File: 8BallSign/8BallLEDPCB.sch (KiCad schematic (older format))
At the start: 42 parts, among them J101 Solder pads, J102 Solder pads

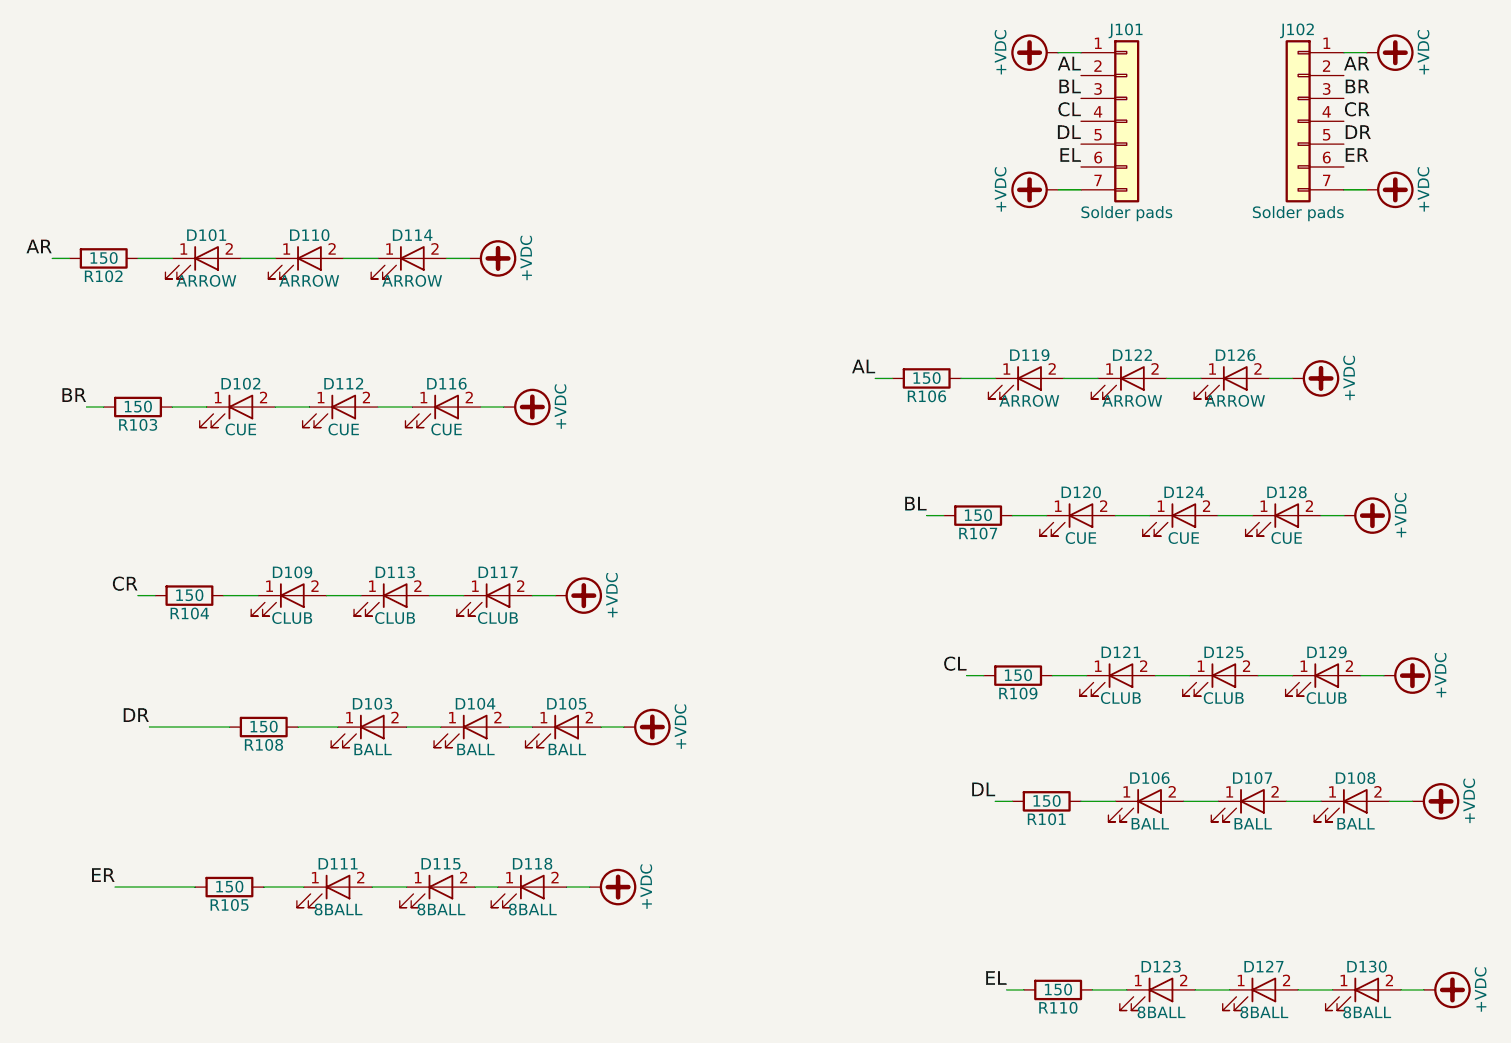
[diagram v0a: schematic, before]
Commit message: Single PCB version (thinner sign).
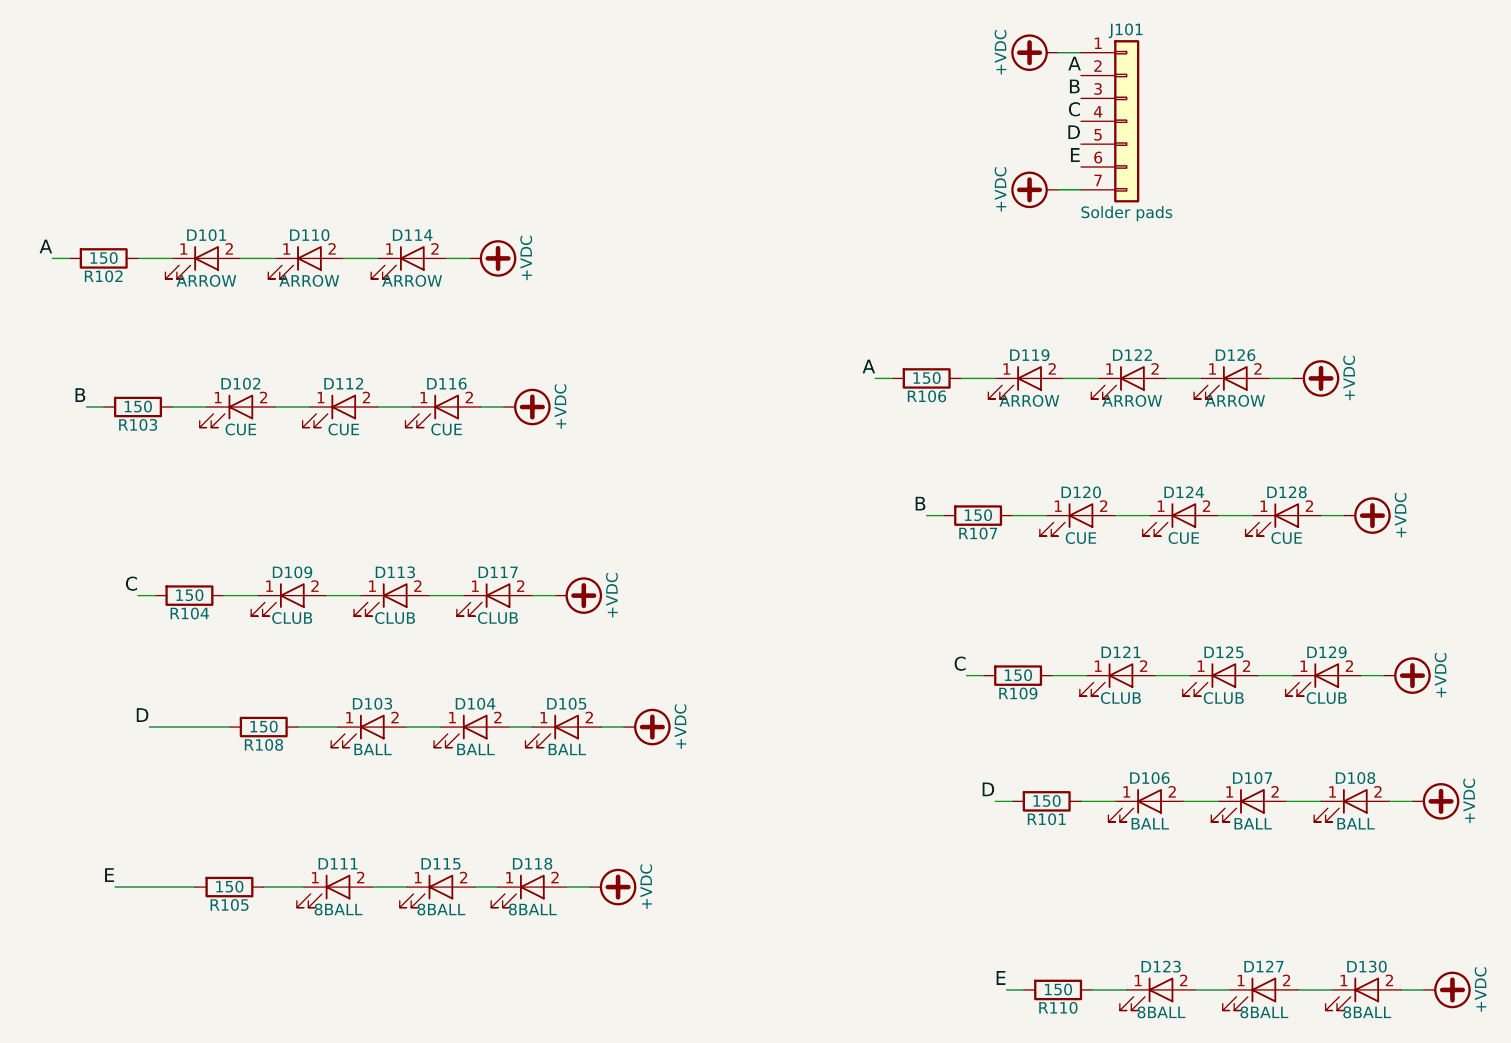
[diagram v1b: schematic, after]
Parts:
- removed J102: Solder pads, SolderPads:PowerPlus5, symbol Conn_01x07
- J101: footprint SolderPads:PowerPlus5 -> SolderPads:PowerPlus5X2
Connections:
- net AR is gone; now on net A: R102.2
- net BR is gone; now on net B: R103.2
- net CR is gone; now on net C: R104.2
- net DR is gone; now on net D: R108.2
- net ER is gone; now on net E: R105.2
- net AL renamed A
- net BL renamed B
- net CL renamed C
- net DL renamed D
- net EL renamed E
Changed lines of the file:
@@
 LIBS:contrib
 LIBS:valves
-LIBS:tbd62x83a
-LIBS:led_3in1
 LIBS:8BallLEDPCB-cache
 EELAYER 25 0
@@
 F 0 "J101" H 8150 1925 50  0000 C CNN
 F 1 "Solder pads" H 8150 1125 50  0000 C CNN
-F 2 "SolderPads:PowerPlus5" H 8150 1525 50  0001 C CNN
+F 2 "SolderPads:PowerPlus5X2" H 8150 1525 50  0001 C CNN
 F 3 "" H 8150 1525 50  0001 C CNN
 	1    8150 1525
@@
 $EndComp
 $Comp
-L +VDC #PWR02
+L +VDC #PWR01
 U 1 1 63DE8BD5
 P 7850 1225
-F 0 "#PWR02" H 7850 1125 50  0001 C CNN
+F 0 "#PWR01" H 7850 1125 50  0001 C CNN
 F 1 "+VDC" H 7850 1475 50  0000 C CNN
 F 2 "" H 7850 1225 50  0001 C CNN
@@
 	0    -1   -1   0
 $EndComp
-$Comp
-L Conn_01x07 J102
-U 1 1 63DE8C4C
-P 8900 1525
-F 0 "J102" H 8900 1925 50  0000 C CNN
-F 1 "Solder pads" H 8900 1125 50  0000 C CNN
-F 2 "SolderPads:PowerPlus5" H 8900 1525 50  0001 C CNN
-F 3 "" H 8900 1525 50  0001 C CNN
-	1    8900 1525
-	-1   0    0    -1
-$EndComp
-$Comp
-L +VDC #PWR04
-U 1 1 63DE8C59
-P 9200 1225
-F 0 "#PWR04" H 9200 1125 50  0001 C CNN
-F 1 "+VDC" H 9200 1475 50  0000 C CNN
-F 2 "" H 9200 1225 50  0001 C CNN
-F 3 "" H 9200 1225 50  0001 C CNN
-	1    9200 1225
-	0    1    -1   0
-$EndComp
 Text Label 7950 1325 2    60   ~ 0
-AL
-Text Label 9100 1325 0    60   ~ 0
-AR
+A
 Text Label 7950 1425 2    60   ~ 0
-BL
+B
 Text Label 7950 1525 2    60   ~ 0
-CL
+C
 Text Label 7950 1625 2    60   ~ 0
-DL
+D
 Text Label 7950 1725 2    60   ~ 0
-EL
-Text Label 9100 1425 0    60   ~ 0
-BR
-Text Label 9100 1525 0    60   ~ 0
-CR
-Text Label 9100 1625 0    60   ~ 0
-DR
-Text Label 9100 1725 0    60   ~ 0
-ER
+E
 Text Label 7050 2650 2    60   ~ 0
-AL
+A
 Text Label 7275 3250 2    60   ~ 0
-BL
+B
 Text Label 7450 3950 2    60   ~ 0
-CL
+C
 Text Label 7575 4500 2    60   ~ 0
-DL
+D
 Text Label 7625 5325 2    60   ~ 0
-EL
+E
 Text Label 3450 2125 2    60   ~ 0
-AR
+A
 Text Label 3600 2775 2    60   ~ 0
-BR
+B
 Text Label 3825 3600 2    60   ~ 0
-CR
+C
 Text Label 3875 4175 2    60   ~ 0
-DR
+D
 Text Label 3725 4875 2    60   ~ 0
-ER
+E
 $Comp
 L R R108
@@
 	7850 1225 7950 1225
 Wire Wire Line
-	9100 1825 9200 1825
-Wire Wire Line
-	9200 1225 9100 1225
-Wire Wire Line
 	7575 4500 7650 4500
 Wire Wire Line
@@
 	5450 4175 5550 4175
 $Comp
-L +VDC #PWR05
+L +VDC #PWR02
 U 1 1 63DEF385
 P 5950 4175
-F 0 "#PWR05" H 5950 4075 50  0001 C CNN
+F 0 "#PWR02" H 5950 4075 50  0001 C CNN
 F 1 "+VDC" H 5950 4425 50  0000 C CNN
 F 2 "" H 5950 4175 50  0001 C CNN
@@
 	8850 4500 9000 4500
 $Comp
-L +VDC #PWR06
+L +VDC #PWR03
 U 1 1 63DEFC3C
 P 9400 4500
-F 0 "#PWR06" H 9400 4400 50  0001 C CNN
+F 0 "#PWR03" H 9400 4400 50  0001 C CNN
 F 1 "+VDC" H 9400 4750 50  0000 C CNN
 F 2 "" H 9400 4500 50  0001 C CNN
@@
 	8900 5325 9050 5325
 $Comp
-L +VDC #PWR07
+L +VDC #PWR04
 U 1 1 63DF4D04
 P 9450 5325
-F 0 "#PWR07" H 9450 5225 50  0001 C CNN
+F 0 "#PWR04" H 9450 5225 50  0001 C CNN
 F 1 "+VDC" H 9450 5575 50  0000 C CNN
 F 2 "" H 9450 5325 50  0001 C CNN
@@
 	5300 4875 5400 4875
 $Comp
-L +VDC #PWR08
+L +VDC #PWR05
 U 1 1 63DF5057
 P 5800 4875
-F 0 "#PWR08" H 5800 4775 50  0001 C CNN
+F 0 "#PWR05" H 5800 4775 50  0001 C CNN
 F 1 "+VDC" H 5800 5125 50  0000 C CNN
 F 2 "" H 5800 4875 50  0001 C CNN
@@
 	8725 3950 8875 3950
 $Comp
-L +VDC #PWR09
+L +VDC #PWR06
 U 1 1 63DF58CC
 P 9275 3950
-F 0 "#PWR09" H 9275 3850 50  0001 C CNN
+F 0 "#PWR06" H 9275 3850 50  0001 C CNN
 F 1 "+VDC" H 9275 4200 50  0000 C CNN
 F 2 "" H 9275 3950 50  0001 C CNN
@@
 	5100 3600 5250 3600
 $Comp
-L +VDC #PWR010
+L +VDC #PWR07
 U 1 1 63DF5E11
 P 5650 3600
-F 0 "#PWR010" H 5650 3500 50  0001 C CNN
+F 0 "#PWR07" H 5650 3500 50  0001 C CNN
 F 1 "+VDC" H 5650 3850 50  0000 C CNN
 F 2 "" H 5650 3600 50  0001 C CNN
@@
 	4875 2775 5025 2775
 $Comp
-L +VDC #PWR011
+L +VDC #PWR08
 U 1 1 63DF64F8
 P 5425 2775
-F 0 "#PWR011" H 5425 2675 50  0001 C CNN
+F 0 "#PWR08" H 5425 2675 50  0001 C CNN
 F 1 "+VDC" H 5425 3025 50  0000 C CNN
 F 2 "" H 5425 2775 50  0001 C CNN
@@
 	4725 2125 4875 2125
 $Comp
-L +VDC #PWR012
+L +VDC #PWR09
 U 1 1 63DF676F
 P 5275 2125
-F 0 "#PWR012" H 5275 2025 50  0001 C CNN
+F 0 "#PWR09" H 5275 2025 50  0001 C CNN
 F 1 "+VDC" H 5275 2375 50  0000 C CNN
 F 2 "" H 5275 2125 50  0001 C CNN
@@
 	8550 3250 8700 3250
 $Comp
-L +VDC #PWR013
+L +VDC #PWR010
 U 1 1 63DF6A2A
 P 9100 3250
-F 0 "#PWR013" H 9100 3150 50  0001 C CNN
+F 0 "#PWR010" H 9100 3150 50  0001 C CNN
 F 1 "+VDC" H 9100 3500 50  0000 C CNN
 F 2 "" H 9100 3250 50  0001 C CNN
@@
 	8325 2650 8475 2650
 $Comp
-L +VDC #PWR014
+L +VDC #PWR011
 U 1 1 63DF6C9E
 P 8875 2650
-F 0 "#PWR014" H 8875 2550 50  0001 C CNN
+F 0 "#PWR011" H 8875 2550 50  0001 C CNN
 F 1 "+VDC" H 8875 2900 50  0000 C CNN
 F 2 "" H 8875 2650 50  0001 C CNN
@@
 	8775 2650 8875 2650
 $Comp
-L +VDC #PWR?
-U 1 1 63DF8C38
-P 9200 1825
-F 0 "#PWR?" H 9200 1725 50  0001 C CNN
-F 1 "+VDC" H 9200 2075 50  0000 C CNN
-F 2 "" H 9200 1825 50  0001 C CNN
-F 3 "" H 9200 1825 50  0001 C CNN
-	1    9200 1825
-	0    1    -1   0
-$EndComp
-$Comp
-L +VDC #PWR?
+L +VDC #PWR012
 U 1 1 63DF8DA3
 P 7850 1825
-F 0 "#PWR?" H 7850 1725 50  0001 C CNN
+F 0 "#PWR012" H 7850 1725 50  0001 C CNN
 F 1 "+VDC" H 7850 2075 50  0000 C CNN
 F 2 "" H 7850 1825 50  0001 C CNN
